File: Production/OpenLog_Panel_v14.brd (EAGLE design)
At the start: 232.7 x 111 mm, 1323 parts, among them Q1 16MHZ, Q10 16MHZ, Q11 16MHZ, Q12 16MHZ, Q13 16MHZ, Q14 16MHZ, Q15 16MHZ, Q16 16MHZ, Q17 16MHZ, Q18 16MHZ, Q19 16MHZ, Q2 16MHZ, Q20 16MHZ, Q21 16MHZ, Q22 16MHZ, Q23 16MHZ, Q24 16MHZ, Q25 16MHZ, Q26 16MHZ, Q27 16MHZ, Q28 16MHZ, Q29 16MHZ, Q3 16MHZ, Q30 16MHZ, Q31 16MHZ, Q32 16MHZ, Q33 16MHZ, Q34 16MHZ, Q35 16MHZ, Q36 16MHZ, Q37 16MHZ, Q38 16MHZ, Q39 16MHZ, Q4 16MHZ, Q40 16MHZ, Q41 16MHZ, Q42 16MHZ, Q43 16MHZ, Q44 16MHZ, Q45 16MHZ, Q46 16MHZ, Q47 16MHZ, Q48 16MHZ, Q49 16MHZ, Q5 16MHZ, Q50 16MHZ, Q51 16MHZ, Q52 16MHZ, Q53 16MHZ, Q54 16MHZ, Q55 16MHZ, Q56 16MHZ, Q57 16MHZ, Q58 16MHZ, Q59 16MHZ, Q6 16MHZ, Q60 16MHZ, Q7 16MHZ, Q8 16MHZ, Q9 16MHZ, U1 ATMEGA328P_TQFP, U10 3.3V MIC5205, U100 3.3V MIC5205, U101 microSD Socket, U102 ATMEGA328P_TQFP, U103 3.3V MIC5205, U104 microSD Socket, U105 ATMEGA328P_TQFP, U106 3.3V MIC5205, U107 microSD Socket, U108 ATMEGA328P_TQFP, U109 3.3V MIC5205, U11 microSD Socket, U110 microSD Socket, U111 ATMEGA328P_TQFP, U112 3.3V MIC5205, U113 microSD Socket, U114 ATMEGA328P_TQFP, U115 3.3V MIC5205, U116 microSD Socket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

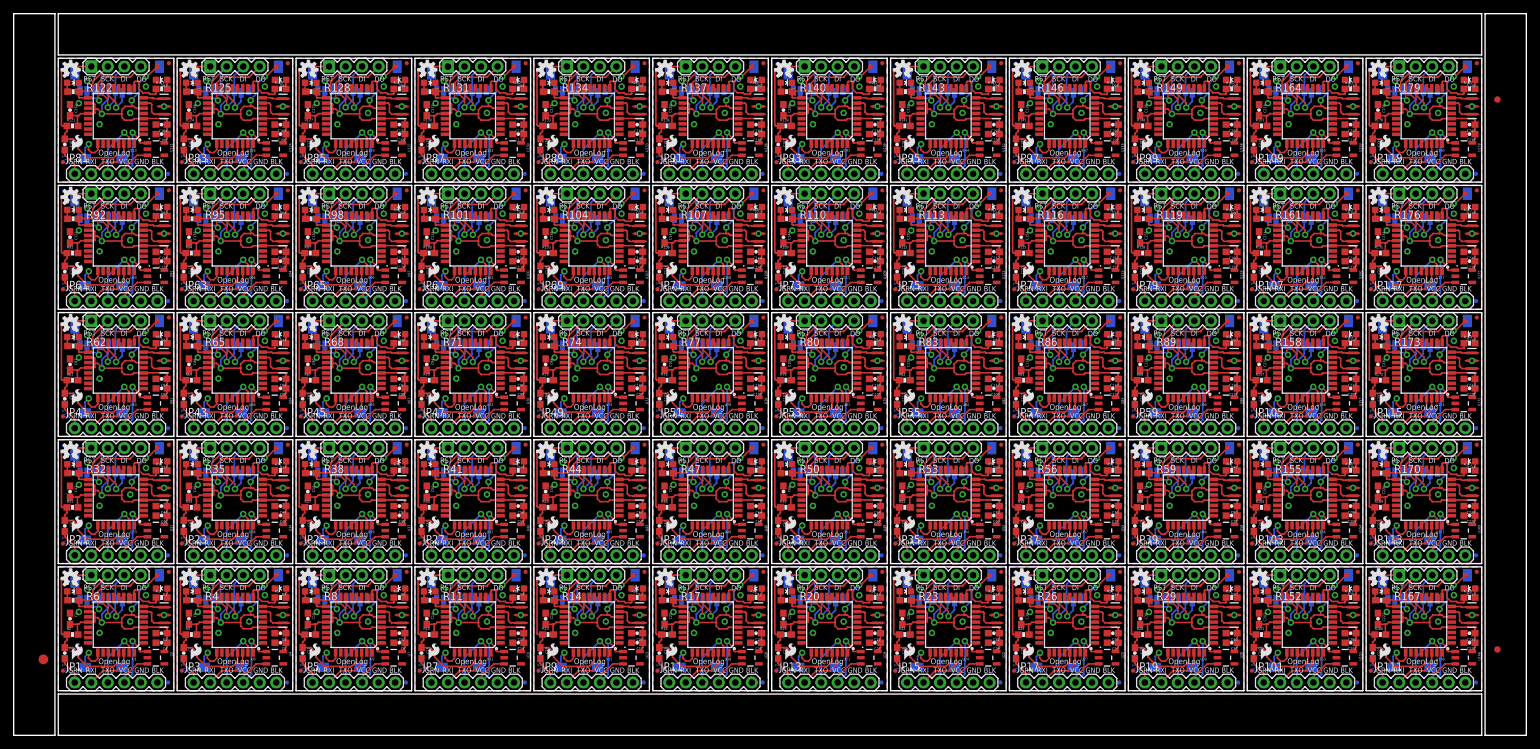
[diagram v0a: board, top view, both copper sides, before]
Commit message: added bottom side panel fids
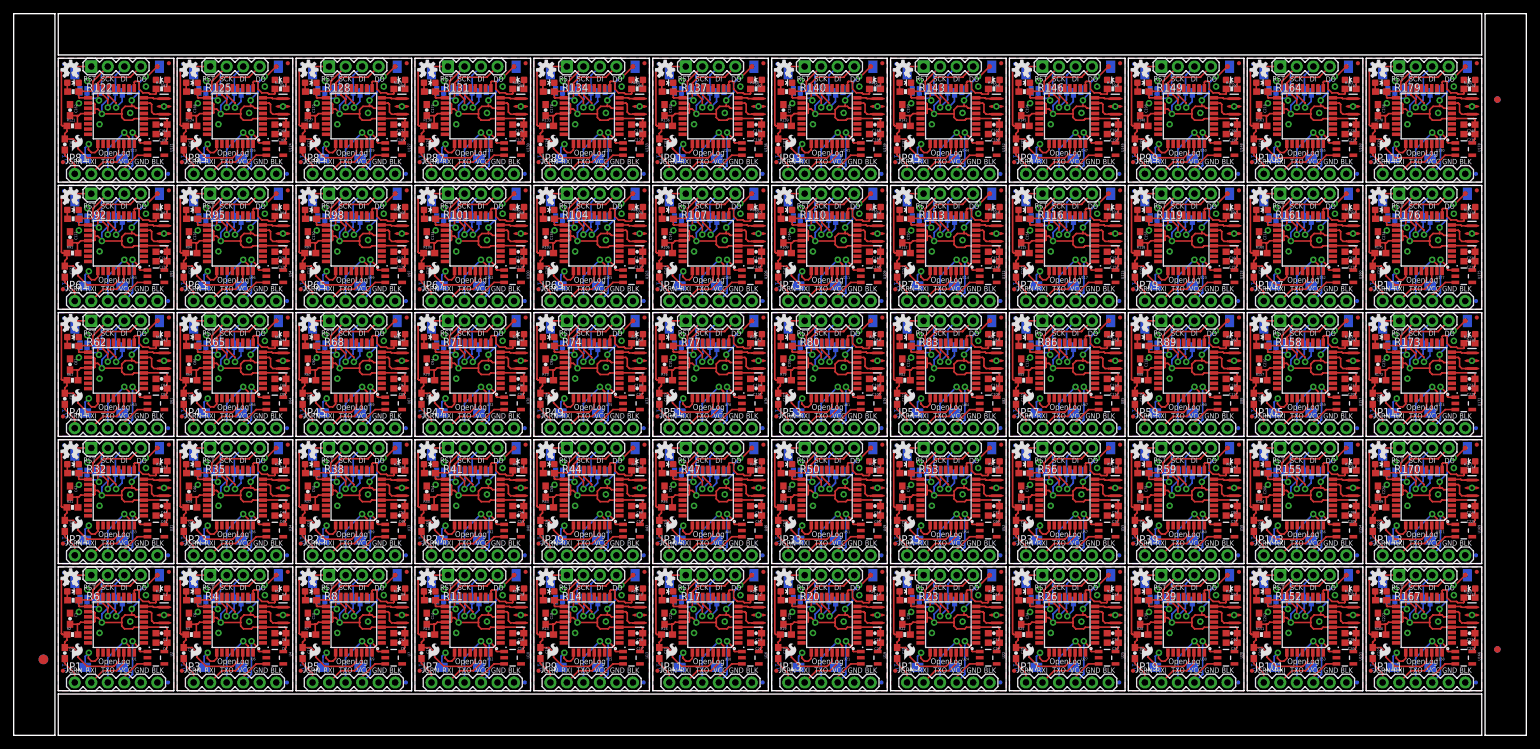
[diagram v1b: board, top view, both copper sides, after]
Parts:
- added E$2: (no value), SparkFun-Retired:FIDUCIAL-1.5X3
- added E$3, E$4: (no value), SparkFun-Aesthetics:FIDUCIAL-1X2
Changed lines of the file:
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@@
 <element name="FID239" library="SparkFun-Aesthetics" package="MICRO-FIDUCIAL" value="FIDUCIALUFIDUCIAL" x="224.917" y="86.36" smashed="yes" rot="MR0"/>
 <element name="FID240" library="SparkFun-Aesthetics" package="MICRO-FIDUCIAL" value="FIDUCIALUFIDUCIAL" x="208.915" y="103.251" smashed="yes" rot="MR0"/>
+<element name="E$2" library="SparkFun-Retired" package="FIDUCIAL-1.5X3" value="" x="4.572" y="11.684" rot="MR0"/>
+<element name="E$3" library="SparkFun-Aesthetics" package="FIDUCIAL-1X2" value="" x="228.219" y="13.208" rot="MR0"/>
+<element name="E$4" library="SparkFun-Aesthetics" package="FIDUCIAL-1X2" value="" x="228.219" y="97.79" rot="MR180"/>
 </elements>
 <signals>
